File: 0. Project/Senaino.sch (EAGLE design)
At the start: 37 parts, among them Q1 16 MHz, Q2 12 MHz, U1 ATMEGA328P-PU, U3 7805T, U4 CH340G, X1 POWERSUPPLY_DC21MMX

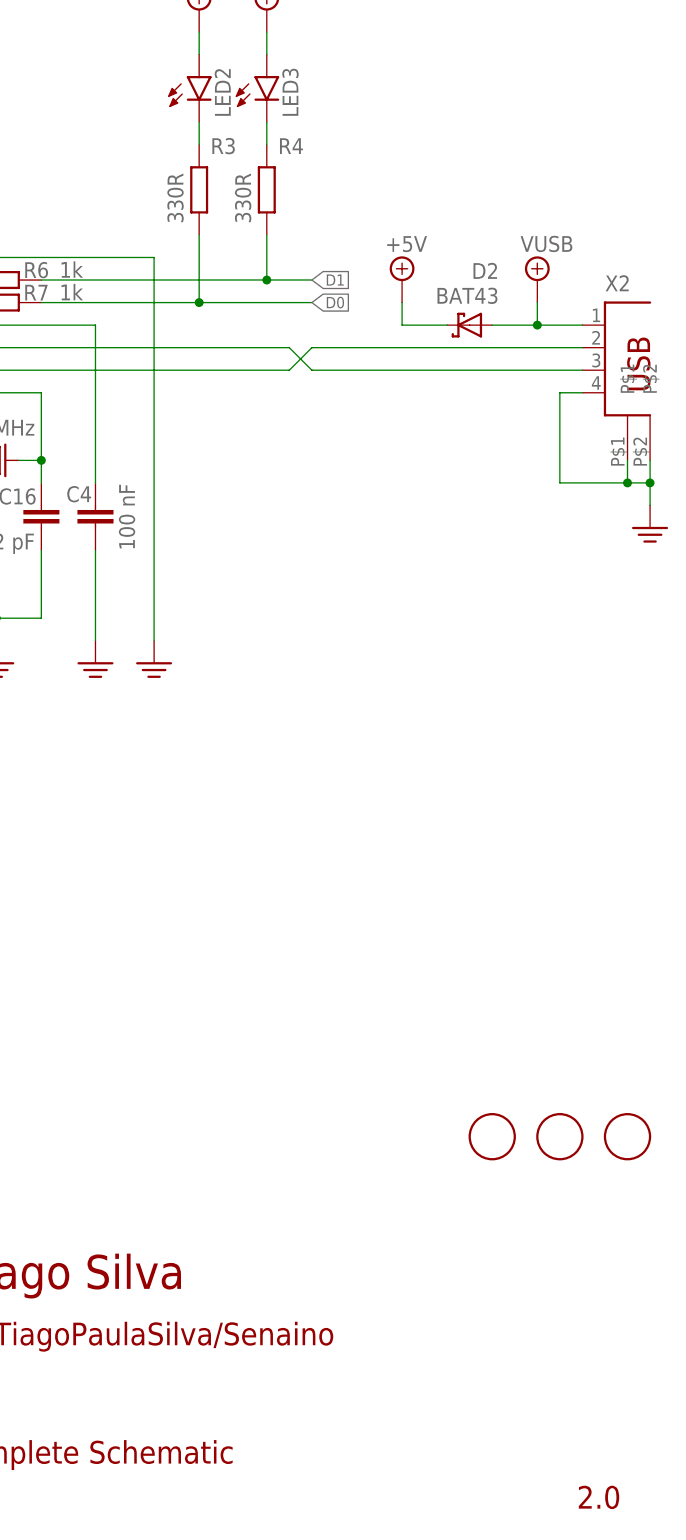
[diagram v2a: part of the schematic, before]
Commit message: pin 1 from CH340 added to GND & R3/R4 changed to 1k
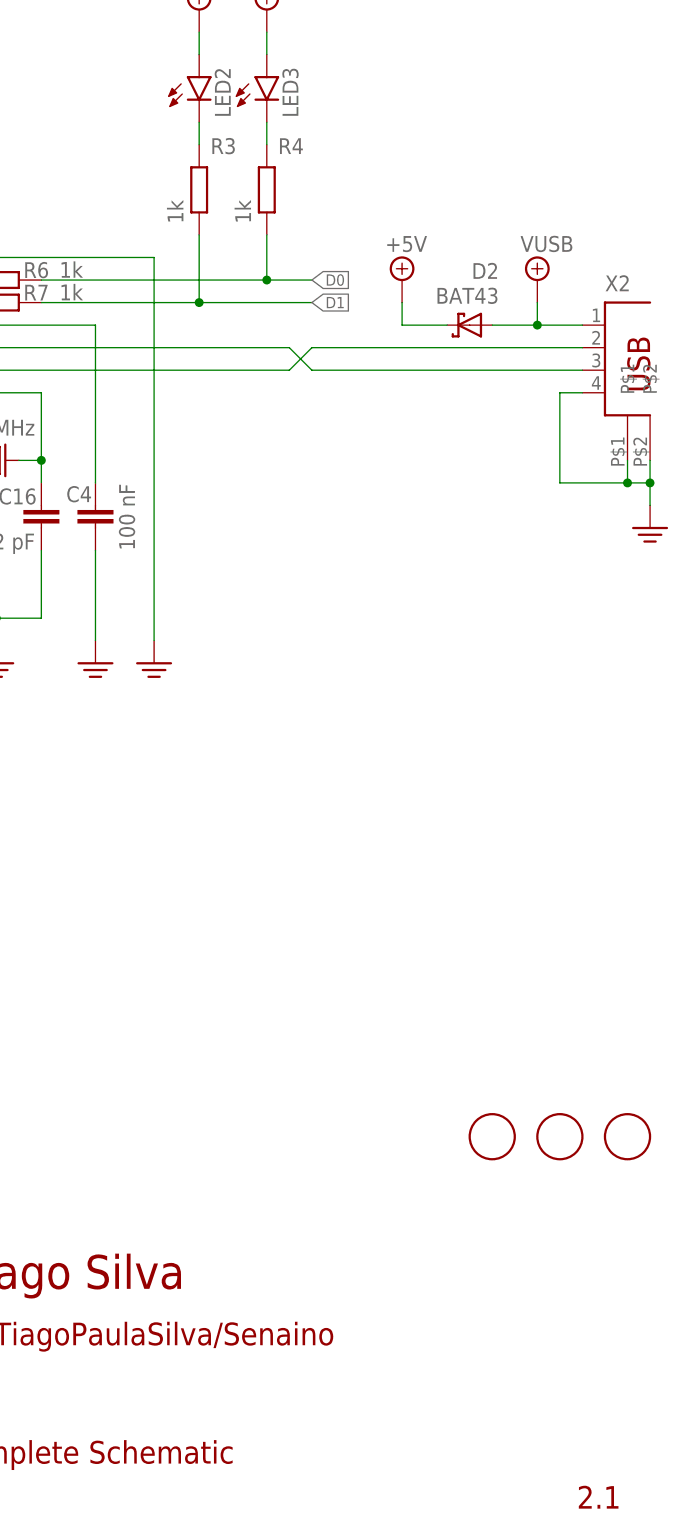
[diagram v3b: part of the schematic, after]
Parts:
- R3, R4: value 330R -> 1k
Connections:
- removed net PE: U4.GND
- net D0: now also R4.1, R6.2; no longer R3.1, R7.2
- net D1: now also R3.1, R7.2; no longer R4.1, R6.2
- net GND: now also U4.GND
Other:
- note added: "2.1"
- note removed: "2.0"
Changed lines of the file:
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@@
 <?xml version="1.0" encoding="utf-8"?>
 <!DOCTYPE eagle SYSTEM "eagle.dtd">
-<eagle version="9.4.2">
+<eagle version="9.5.1">
 <drawing>
 <settings>
@@
 <part name="C3" library="rcl" library_urn="urn:adsk.eagle:library:334" deviceset="C-EU" device="025-024X044" package3d_urn="urn:adsk.eagle:package:23630/1" value="100 nF"/>
 <part name="+5V3" library="supply2" library_urn="urn:adsk.eagle:library:372" deviceset="+5V" device=""/>
-<part name="R3" library="rcl" library_urn="urn:adsk.eagle:library:334" deviceset="R-EU_" device="0204/7" package3d_urn="urn:adsk.eagle:package:23498/2" value="330R"/>
+<part name="R3" library="rcl" library_urn="urn:adsk.eagle:library:334" deviceset="R-EU_" device="0204/7" package3d_urn="urn:adsk.eagle:package:23498/2" value="1k"/>
 <part name="LED2" library="led" library_urn="urn:adsk.eagle:library:259" deviceset="LED" device="3MM" package3d_urn="urn:adsk.eagle:package:15797/1"/>
 <part name="+5V5" library="supply2" library_urn="urn:adsk.eagle:library:372" deviceset="+5V" device=""/>
-<part name="R4" library="rcl" library_urn="urn:adsk.eagle:library:334" deviceset="R-EU_" device="0204/7" package3d_urn="urn:adsk.eagle:package:23498/2" value="330R"/>
+<part name="R4" library="rcl" library_urn="urn:adsk.eagle:library:334" deviceset="R-EU_" device="0204/7" package3d_urn="urn:adsk.eagle:package:23498/2" value="1k"/>
 <part name="LED3" library="led" library_urn="urn:adsk.eagle:library:259" deviceset="LED" device="3MM" package3d_urn="urn:adsk.eagle:package:15797/1"/>
 <part name="+5V6" library="supply2" library_urn="urn:adsk.eagle:library:372" deviceset="+5V" device=""/>
@@
 <text x="183.515" y="26.035" size="3.81" layer="94">Tiago Silva</text>
 <text x="168.91" y="19.685" size="2.54" layer="94">github.com/TiagoPaulaSilva/Senaino</text>
-<text x="253.365" y="1.27" size="2.54" layer="94" ratio="5">2.0</text>
+<text x="253.365" y="1.27" size="2.54" layer="94" ratio="5">2.1</text>
 <text x="182.245" y="6.35" size="2.54" layer="94" ratio="5">Complete Schematic</text>
 </plain>
@@
 <junction x="187.96" y="101.6"/>
 </segment>
+<segment>
+<pinref part="U4" gate="U1" pin="GND"/>
+<wire x1="180.34" y1="142.24" x2="205.74" y2="142.24" width="0.1524" layer="91"/>
+<wire x1="205.74" y1="142.24" x2="205.74" y2="99.06" width="0.1524" layer="91"/>
+<pinref part="GND7" gate="PE" pin="PE"/>
+</segment>
 </net>
 <net name="D1" class="0">
@@
 <wire x1="147.32" y1="27.94" x2="142.24" y2="27.94" width="0.1524" layer="91"/>
 <label x="142.24" y="27.94" size="1.27" layer="95" rot="R180" xref="yes"/>
+</segment>
+<segment>
+<pinref part="R7" gate="G$1" pin="2"/>
+<wire x1="193.04" y1="137.16" x2="210.82" y2="137.16" width="0.1524" layer="91"/>
+<label x="223.52" y="137.16" size="1.27" layer="95" ratio="5" xref="yes"/>
+<pinref part="R3" gate="G$1" pin="1"/>
+<wire x1="210.82" y1="137.16" x2="223.52" y2="137.16" width="0.1524" layer="91"/>
+<wire x1="210.82" y1="144.78" x2="210.82" y2="137.16" width="0.1524" layer="91"/>
+<junction x="210.82" y="137.16"/>
+</segment>
+</net>
+<net name="D0" class="0">
+<segment>
+<pinref part="U1" gate="G$1" pin="(RXD)PD0"/>
+<wire x1="93.98" y1="25.4" x2="109.22" y2="25.4" width="0.1524" layer="91"/>
+<label x="109.22" y="25.4" size="1.27" layer="95" xref="yes"/>
+</segment>
+<segment>
+<pinref part="DIGITAL1" gate="A" pin="1"/>
+<wire x1="147.32" y1="25.4" x2="142.24" y2="25.4" width="0.1524" layer="91"/>
+<label x="142.24" y="25.4" size="1.27" layer="95" rot="R180" xref="yes"/>
 </segment>
 <segment>
@@
 <wire x1="218.44" y1="144.78" x2="218.44" y2="139.7" width="0.1524" layer="91"/>
 <junction x="218.44" y="139.7"/>
-</segment>
-</net>
-<net name="D0" class="0">
-<segment>
-<pinref part="U1" gate="G$1" pin="(RXD)PD0"/>
-<wire x1="93.98" y1="25.4" x2="109.22" y2="25.4" width="0.1524" layer="91"/>
-<label x="109.22" y="25.4" size="1.27" layer="95" xref="yes"/>
-</segment>
-<segment>
-<pinref part="DIGITAL1" gate="A" pin="1"/>
-<wire x1="147.32" y1="25.4" x2="142.24" y2="25.4" width="0.1524" layer="91"/>
-<label x="142.24" y="25.4" size="1.27" layer="95" rot="R180" xref="yes"/>
-</segment>
-<segment>
-<pinref part="R7" gate="G$1" pin="2"/>
-<wire x1="193.04" y1="137.16" x2="210.82" y2="137.16" width="0.1524" layer="91"/>
-<label x="223.52" y="137.16" size="1.27" layer="95" ratio="5" xref="yes"/>
-<pinref part="R3" gate="G$1" pin="1"/>
-<wire x1="210.82" y1="137.16" x2="223.52" y2="137.16" width="0.1524" layer="91"/>
-<wire x1="210.82" y1="144.78" x2="210.82" y2="137.16" width="0.1524" layer="91"/>
-<junction x="210.82" y="137.16"/>
 </segment>
 </net>
@@
 </segment>
 </net>
-<net name="PE" class="0">
-<segment>
-<pinref part="U4" gate="U1" pin="GND"/>
-<wire x1="180.34" y1="142.24" x2="205.74" y2="142.24" width="0.1524" layer="91"/>
-<wire x1="205.74" y1="142.24" x2="205.74" y2="99.06" width="0.1524" layer="91"/>
-<pinref part="GND7" gate="PE" pin="PE"/>
-</segment>
-</net>
